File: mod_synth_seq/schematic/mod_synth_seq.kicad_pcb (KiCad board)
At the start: 2 copper layers, 100.3 x 132.1 mm, 88 parts, among them J1 CV1, J10 Step 8 Gate, J11 Reset, J12 Clock, J13 Gate Out, J2 CV2, J3 Step 1 Gate, J4 Step 2 Gate, J5 Step 3 Gate, J6 Step 4 Gate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

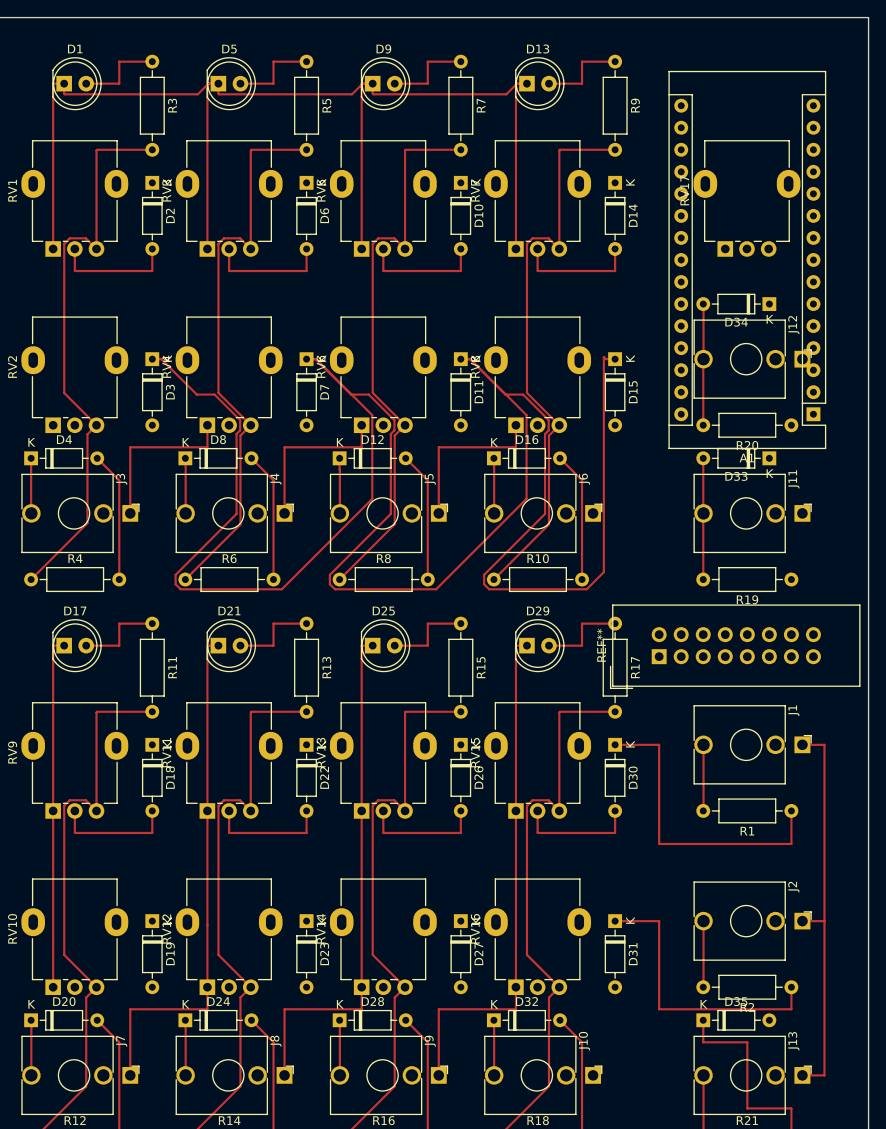
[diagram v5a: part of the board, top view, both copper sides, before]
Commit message: Running out of places for tracks
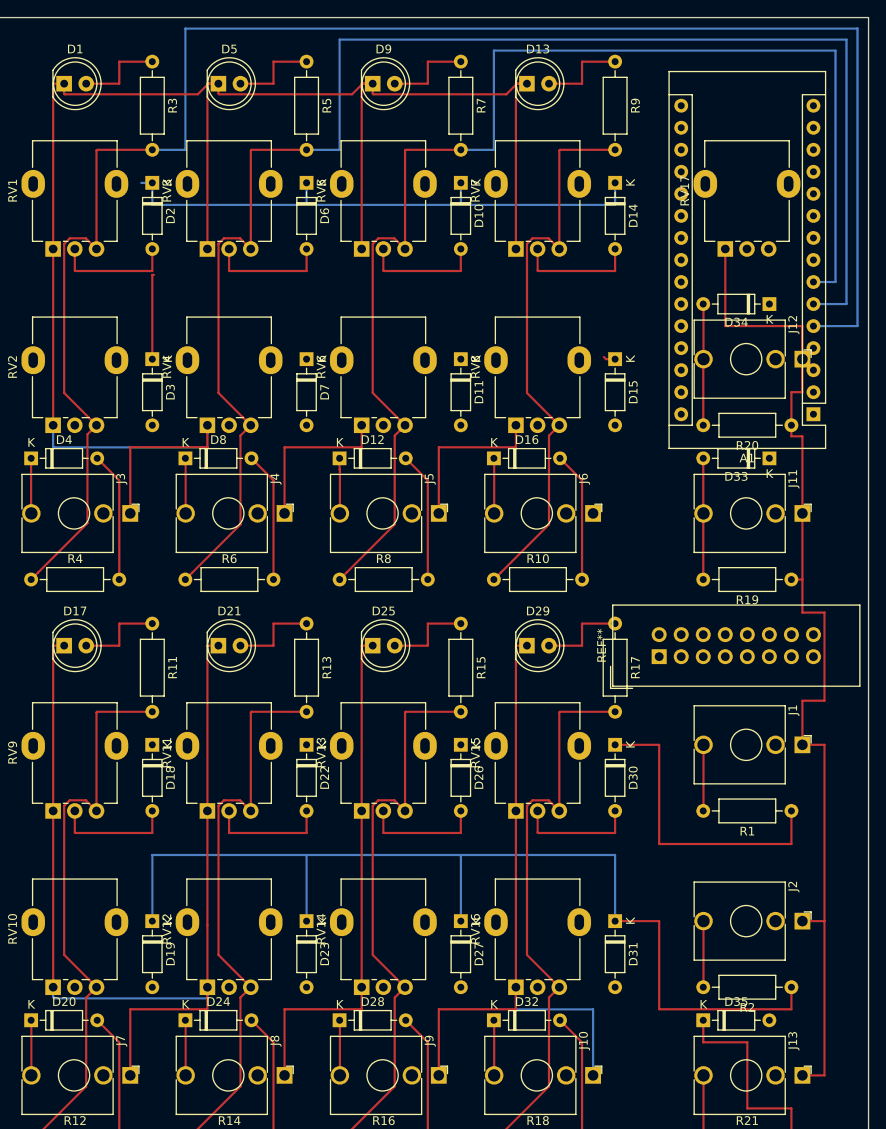
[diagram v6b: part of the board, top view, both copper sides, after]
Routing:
- net GND: track 462.3 -> 619.7 mm
- net Net-(D11-Pad1): track 273.4 -> 128.1 mm
- net Net-(A1-Pad5): track 65.7 -> 200.3 mm
- net Net-(A1-Pad6): track 65.7 -> 174.9 mm
- net Net-(A1-Pad7): track 65.7 -> 149.5 mm
- net Net-(D10-Pad1): track 35.6 -> 100.3 mm
